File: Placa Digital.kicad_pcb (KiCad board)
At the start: 2 copper layers, 60 x 80 mm, 23 parts, among them J1 Entradas / Salidas, Q1 BC548, Q2 BC548, U1 EC11_Module, U2 Alimentación, U3 ST7920_Display, U4 10K

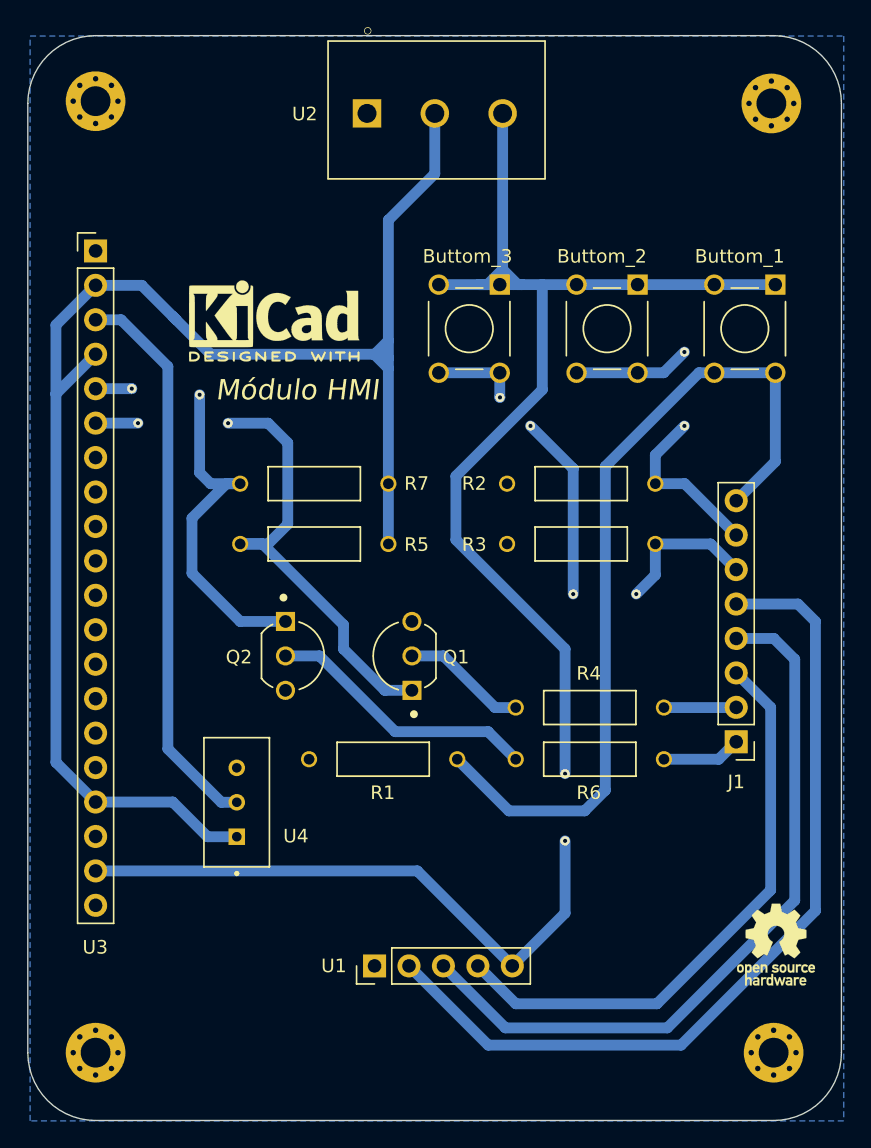
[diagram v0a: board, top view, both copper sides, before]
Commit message: Replacement consider control module
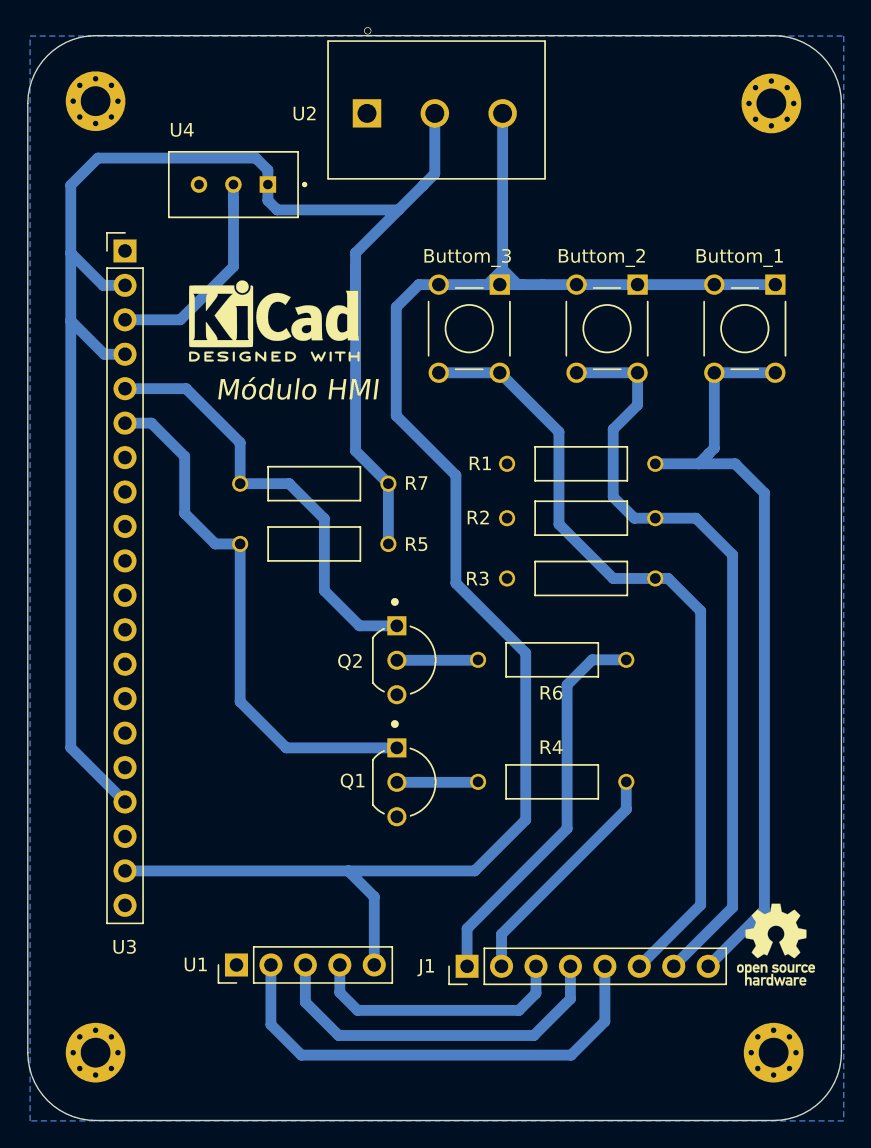
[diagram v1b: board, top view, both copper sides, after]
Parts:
- moved U4 45.6 mm to (125.6, 70.3), turned to 180 degrees
- moved R1 26.2 mm to (151.3, 90.9)
- moved J1 25.8 mm to (142.8, 127.9), turned to 90 degrees
- moved U1 10.2 mm to (125.8, 127.8)
- moved Q1 9.34 mm to (138.5, 114.4), turned to -90 degrees
- moved Q2 8.22 mm to (138.5, 105.4)
- moved R6 7.84 mm to (149.1, 105.3)
- moved R4 6.14 mm to (149.1, 114.3)
- moved R2 2.55 mm to (151.3, 94.9)
- moved R3 2.55 mm to (151.3, 99.3)
- moved U3 2.17 mm to (117.6, 75.2)
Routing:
- net /toMicroC_Button2: track 21.3 -> 57.1 mm, vias 2 -> 0
- net /toMicroC_EncoderSignalA: track 64.2 -> 35.1 mm
- net /toMicroC_EncoderSignalB: track 54.4 -> 26.8 mm
- net /toMicroC_Button3: track 31.1 -> 58.7 mm, vias 4 -> 0
- net Net-(U3-Pad3): track 41.7 -> 16.2 mm
- net /toMicroC_EncoderButton: track 43.3 -> 19.6 mm
- net /fromMicroC_DisplaySID: track 5.86 -> 28.9 mm
- net Net-(Q2-Pad2): track 20.1 -> 6.00 mm
- net /fromMicroC_DisplaySCLK: track 5.34 -> 17.4 mm
- net +5V: track 116.3 -> 123.2 mm
- net /toMicroC_Button1: track 63.0 -> 57.2 mm
- net Net-(Q2-Pad1): track 28.8 -> 32.2 mm, vias 2 -> 0
- net Net-(Q1-Pad2): track 9.33 -> 6.00 mm
- net Net-(Q1-Pad1): track 36.4 -> 39.2 mm, vias 2 -> 0
- net +3V3: track 131.6 -> 129.5 mm, vias 2 -> 0

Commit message: Layout modified + Gerbers generated
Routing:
- net Net-(U3-Pad3): track 16.2 -> 23.7 mm
- net +5V: track 123.2 -> 128.5 mm
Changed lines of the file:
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@@
   (segment (start 143.61879 105.35221) (end 143.652 105.319) (width 0.8) (layer "B.Cu") (net 23))
   (segment (start 137.6645 105.35221) (end 143.61879 105.35221) (width 0.8) (layer "B.Cu") (net 23))
-  (segment (start 125.612 71.864) (end 125.617 71.869) (width 0.8) (layer "B.Cu") (net 24))
-  (segment (start 125.612 70.269) (end 125.612 71.864) (width 0.8) (layer "B.Cu") (net 24))
-  (segment (start 121.692 80.244) (end 125.617 76.319) (width 0.8) (layer "B.Cu") (net 24))
-  (segment (start 125.617 71.869) (end 125.617 71.319) (width 0.8) (layer "B.Cu") (net 24))
-  (segment (start 125.617 76.319) (end 125.617 71.869) (width 0.8) (layer "B.Cu") (net 24))
-  (segment (start 117.617 80.244) (end 121.692 80.244) (width 0.8) (layer "B.Cu") (net 24))
+  (segment (start 115.367 72.369) (end 119.917 67.819) (width 0.8) (layer "B.Cu") (net 24))
+  (segment (start 115.367 77.994) (end 115.367 72.369) (width 0.8) (layer "B.Cu") (net 24))
+  (segment (start 125.612 68.764) (end 124.667 67.819) (width 0.8) (layer "B.Cu") (net 24))
+  (segment (start 117.617 80.244) (end 115.367 77.994) (width 0.8) (layer "B.Cu") (net 24))
+  (segment (start 122.917 67.819) (end 122.017 67.819) (width 0.8) (layer "B.Cu") (net 24))
+  (segment (start 119.917 67.819) (end 122.917 67.819) (width 0.8) (layer "B.Cu") (net 24))
+  (segment (start 125.612 70.269) (end 125.612 68.764) (width 0.8) (layer "B.Cu") (net 24))
+  (segment (start 124.667 67.819) (end 122.917 67.819) (width 0.8) (layer "B.Cu") (net 24))
+  (segment (start 128.152 69.204) (end 125.492 66.544) (width 0.8) (layer "B.Cu") (net 26))
+  (segment (start 120.667 81.394) (end 120.667 80.919) (width 0.8) (layer "B.Cu") (net 26))
   (segment (start 128.8395 72.1415) (end 137.7895 72.1415) (width 0.8) (layer "B.Cu") (net 26))
   (segment (start 140.462 65.024) (end 140.462 69.469) (width 0.8) (layer "B.Cu") (net 26))
+  (segment (start 120.667 79.019) (end 120.667 80.919) (width 0.8) (layer "B.Cu") (net 26))
   (segment (start 113.617 80.319) (end 113.617 75.319) (width 0.8) (layer "B.Cu") (net 26))
   (segment (start 140.462 69.469) (end 139.6145 70.3165) (width 0.8) (layer "B.Cu") (net 26))
-  (segment (start 127.267 68.319) (end 115.617 68.319) (width 0.8) (layer "B.Cu") (net 26))
-  (segment (start 117.617 77.704) (end 116.002 77.704) (width 0.8) (layer "B.Cu") (net 26))
+  (segment (start 125.492 66.544) (end 118.842 66.544) (width 0.8) (layer "B.Cu") (net 26))
   (segment (start 137.037 92.329) (end 137.037 96.774) (width 0.8) (layer "B.Cu") (net 26))
-  (segment (start 115.617 68.319) (end 113.617 70.319) (width 0.8) (layer "B.Cu") (net 26))
   (segment (start 117.617 115.804) (end 113.617 111.804) (width 0.8) (layer "B.Cu") (net 26))
   (segment (start 128.152 71.454) (end 128.8395 72.1415) (width 0.8) (layer "B.Cu") (net 26))
-  (segment (start 128.152 70.269) (end 128.152 69.204) (width 0.8) (layer "B.Cu") (net 26))
+  (segment (start 118.842 66.544) (end 113.617 71.769) (width 0.8) (layer "B.Cu") (net 26))
   (segment (start 134.617 89.909) (end 134.617 75.314) (width 0.8) (layer "B.Cu") (net 26))
-  (segment (start 128.152 69.204) (end 127.267 68.319) (width 0.8) (layer "B.Cu") (net 26))
+  (segment (start 117.617 77.704) (end 119.352 77.704) (width 0.8) (layer "B.Cu") (net 26))
   (segment (start 134.617 75.314) (end 137.7895 72.1415) (width 0.8) (layer "B.Cu") (net 26))
+  (segment (start 113.617 71.769) (end 113.617 75.319) (width 0.8) (layer "B.Cu") (net 26))
   (segment (start 117.617 82.784) (end 116.082 82.784) (width 0.8) (layer "B.Cu") (net 26))
   (segment (start 137.037 92.329) (end 134.617 89.909) (width 0.8) (layer "B.Cu") (net 26))
+  (segment (start 119.277 82.784) (end 120.667 81.394) (width 0.8) (layer "B.Cu") (net 26))
+  (segment (start 119.352 77.704) (end 120.667 79.019) (width 0.8) (layer "B.Cu") (net 26))
   (segment (start 134.617 79.319) (end 134.617 76.319) (width 0.8) (layer "B.Cu") (net 26))
   (segment (start 128.152 70.269) (end 128.152 71.454) (width 0.8) (layer "B.Cu") (net 26))
   (segment (start 116.082 82.784) (end 113.617 80.319) (width 0.8) (layer "B.Cu") (net 26))
-  (segment (start 116.002 77.704) (end 113.617 75.319) (width 0.8) (layer "B.Cu") (net 26))
+  (segment (start 117.617 82.784) (end 119.277 82.784) (width 0.8) (layer "B.Cu") (net 26))
   (segment (start 113.617 111.804) (end 113.617 80.319) (width 0.8) (layer "B.Cu") (net 26))
   (segment (start 137.7895 72.1415) (end 139.6145 70.3165) (width 0.8) (layer "B.Cu") (net 26))
-  (segment (start 113.617 70.319) (end 113.617 75.319) (width 0.8) (layer "B.Cu") (net 26))
+  (segment (start 128.152 70.269) (end 128.152 69.204) (width 0.8) (layer "B.Cu") (net 26))
   (zone (net 25) (net_name "GND") (layer "B.Cu") (hatch edge 0.508)
     (connect_pads (clearance 0.508))

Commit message: Version V1 (Clearence)
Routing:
- net +3V3: track 129.5 -> 198.0 mm
- net +5V: track 128.5 -> 175.3 mm
- net Net-(Q1-Pad1): track 39.2 -> 65.7 mm
- net Net-(Q2-Pad1): track 32.2 -> 46.2 mm
- net /toMicroC_Button3: track 58.7 -> 69.4 mm
- net /toMicroC_Button1: track 57.2 -> 67.7 mm
- net Net-(Q1-Pad2): track 6.00 -> 12.0 mm
- net Net-(U3-Pad3): track 23.7 -> 28.5 mm
- net /fromMicroC_DisplaySID: track 28.9 -> 31.5 mm
